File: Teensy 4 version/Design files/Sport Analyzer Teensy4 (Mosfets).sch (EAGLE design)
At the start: 27 parts, among them IC2 7805DT, Q1 MMBT4403, U1 HX711, U2 TXB0108PWR

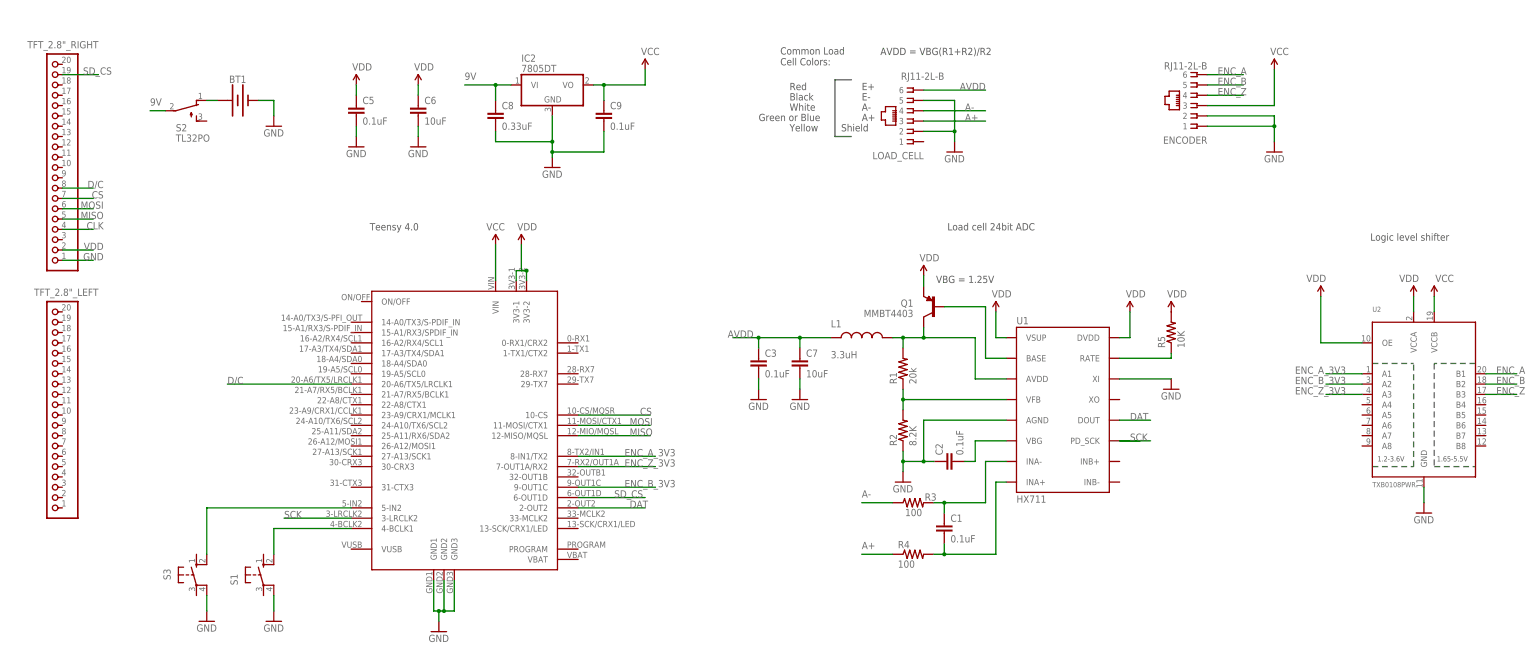
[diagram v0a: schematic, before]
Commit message: Teensy 4 logic level shifters V2
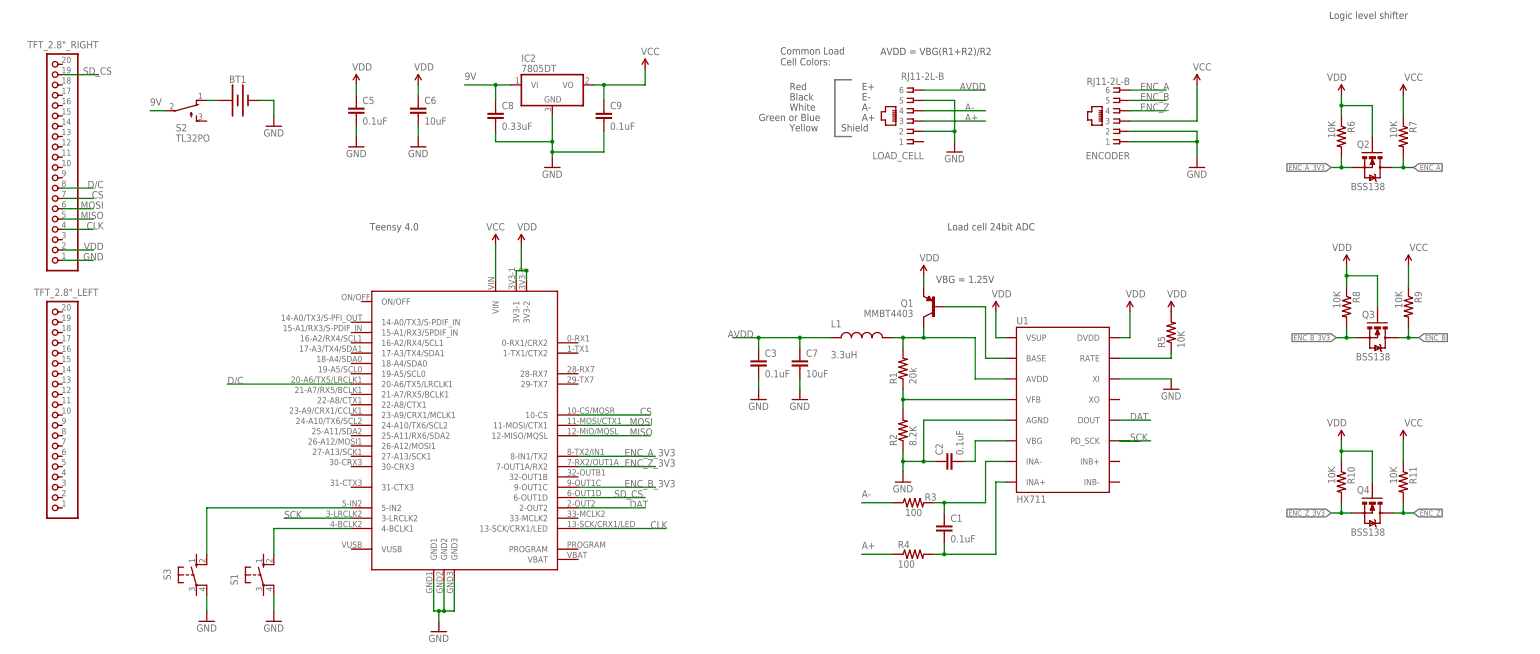
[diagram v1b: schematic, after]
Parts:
- removed U2: TXB0108PWR, microbuilder:TXB0108PWR
- added Q2, Q3, Q4: BSS138, SparkFun:MOSFET-NCHANNELSMD
- added R10, R11, R6, R7, R8, R9: 10K, SparkFun:RESISTOR0603-RES
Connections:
- net CLK: now also U$2.13-SCK/CRX1/LED
- net ENC_A: now also Q2.D, R7.2; no longer U2.B1
- net ENC_A_3V3: now also Q2.S, R6.2; no longer U2.A1
- net ENC_B: now also Q3.D, R9.2; no longer U2.B2
- net ENC_B_3V3: now also Q3.S, R8.2; no longer U2.A2
- net ENC_Z: now also Q4.D, R11.2; no longer U2.B3
- net ENC_Z_3V3: now also Q4.S, R10.2; no longer U2.A3
- net GND: no longer U2.GND
- net VCC: now also R11.1, R7.1, R9.1; no longer U2.VCCB
- net VDD: now also Q2.G, Q3.G, Q4.G, R10.1, R6.1, R8.1; no longer U2.OE, U2.VCCA
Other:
- moved on the sheet: ENCODER
